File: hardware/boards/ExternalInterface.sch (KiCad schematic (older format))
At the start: 1 part

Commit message: Updated part mfr and added the proper part numbers
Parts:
- U?: MFR (none) -> Lattice; MPN (none) -> LFE5UM5G-85F-8BG381I
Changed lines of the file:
@@
 $Descr A4 11693 8268
 encoding utf-8
-Sheet 10 11
+Sheet 9 11
 Title ""
 Date ""
@@
 F 2 "" H 4200 3400 50  0001 C CNN
 F 3 "" H 4200 3400 50  0001 C CNN
+F 4 "Lattice" H 5550 3250 50  0001 C CNN "MFR"
+F 5 "LFE5UM5G-85F-8BG381I" H 5550 3250 50  0001 C CNN "MPN"
 	4    5550 3250
 	1    0    0    -1

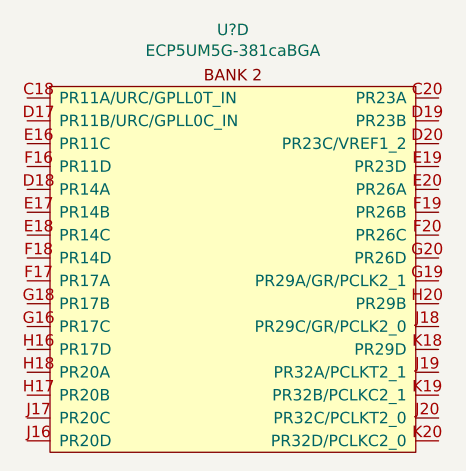
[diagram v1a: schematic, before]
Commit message: Did some annotation and fixed the FPGA bank that was accidentally labled as the cypress part
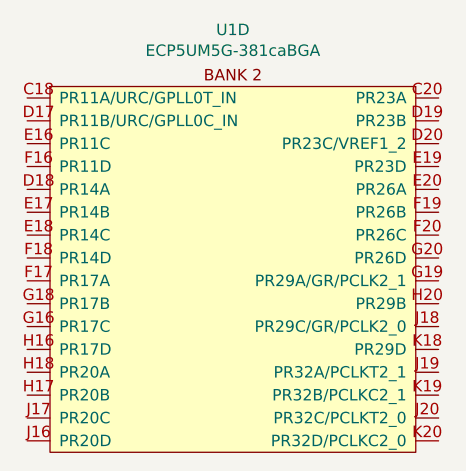
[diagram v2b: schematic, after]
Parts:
- U1: renamed from U?; footprint (none) -> lethalbit:318caBGA
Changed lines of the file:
@@
 $EndDescr
 $Comp
-L lethalbit:ECP5UM5G-381caBGA U?
+L lethalbit:ECP5UM5G-381caBGA U1
 U 4 1 5F2381FE
 P 5550 3250
-F 0 "U?" H 5550 3598 50  0000 C CNN
+F 0 "U1" H 5550 3598 50  0000 C CNN
 F 1 "ECP5UM5G-381caBGA" H 5550 3507 50  0000 C CNN
-F 2 "" H 4200 3400 50  0001 C CNN
+F 2 "lethalbit:318caBGA" H 4200 3400 50  0001 C CNN
 F 3 "" H 4200 3400 50  0001 C CNN
 F 4 "Lattice" H 5550 3250 50  0001 C CNN "MFR"

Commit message: Some more mist schematic edits
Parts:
- U1: DIGIKEY_PN (none) -> 220-2112-ND
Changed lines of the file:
@@
 F 4 "Lattice" H 5550 3250 50  0001 C CNN "MFR"
 F 5 "LFE5UM5G-85F-8BG381I" H 5550 3250 50  0001 C CNN "MPN"
+F 6 "220-2112-ND" H 5550 3250 50  0001 C CNN "DIGIKEY_PN"
 	4    5550 3250
 	1    0    0    -1

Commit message: Some strugglebusting on getting the ERC errors cleaned up a bit
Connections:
- no-connect marks 0 -> 32
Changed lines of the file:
@@
 $Descr A4 11693 8268
 encoding utf-8
-Sheet 9 10
-Title "lethallink"
+Sheet 7 10
+Title "lethallink - External Interface"
 Date "2020-06-13"
 Rev "rev A"
@@
 	1    0    0    -1
 $EndComp
+NoConn ~ 4650 3200
+NoConn ~ 4650 3300
+NoConn ~ 4650 3400
+NoConn ~ 4650 3500
+NoConn ~ 4650 3600
+NoConn ~ 4650 3700
+NoConn ~ 4650 3800
+NoConn ~ 4650 3900
+NoConn ~ 4650 4000
+NoConn ~ 4650 4100
+NoConn ~ 4650 4200
+NoConn ~ 4650 4300
+NoConn ~ 4650 4400
+NoConn ~ 4650 4500
+NoConn ~ 4650 4600
+NoConn ~ 4650 4700
+NoConn ~ 6450 4700
+NoConn ~ 6450 4600
+NoConn ~ 6450 4500
+NoConn ~ 6450 4400
+NoConn ~ 6450 4300
+NoConn ~ 6450 4200
+NoConn ~ 6450 4100
+NoConn ~ 6450 4000
+NoConn ~ 6450 3900
+NoConn ~ 6450 3800
+NoConn ~ 6450 3700
+NoConn ~ 6450 3600
+NoConn ~ 6450 3500
+NoConn ~ 6450 3400
+NoConn ~ 6450 3300
+NoConn ~ 6450 3200
 $EndSCHEMATC
